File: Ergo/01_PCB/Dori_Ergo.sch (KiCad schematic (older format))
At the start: 208 parts, among them J1 TYPE-C-31-M12_13, J2 AVR-ISP-6_mod, J3 4PIN, J4 4PIN, J5 TYPE-C-31-M12_13, J6 AVR-ISP-6_mod, K1 KEYSW, K10 KEYSW, K11 KEYSW, K12 KEYSW, K13 KEYSW, K14 KEYSW, K15 KEYSW, K16 KEYSW, K17 KEYSW, K18 KEYSW, K19 KEYSW, K2 KEYSW, K20 KEYSW, K21 KEYSW, K22 KEYSW, K23 KEYSW, K24 KEYSW, K25 KEYSW, K26 KEYSW, K27 KEYSW, K28 KEYSW, K29 KEYSW, K3 KEYSW, K30 KEYSW, K31 KEYSW, K32 KEYSW, K33 KEYSW, K34 KEYSW, K35 KEYSW, K36 KEYSW, K37 KEYSW, K38 KEYSW, K39 KEYSW, K4 KEYSW, K40 KEYSW, K41 KEYSW, K42 KEYSW, K43 KEYSW, K44 KEYSW, K45 KEYSW, K46 KEYSW, K47 KEYSW, K48 KEYSW, K49 KEYSW, K5 KEYSW, K50 KEYSW, K51 KEYSW, K52 KEYSW, K53 KEYSW, K54 KEYSW, K55 KEYSW, K56 KEYSW, K6 KEYSW, K7 KEYSW, K8 KEYSW, K9 KEYSW, SW1 SW_PUSH, SW10 Rotary_Encoder_Switch, SW2 SW_PUSH, SW3 Rotary_Encoder_Switch, SW4 Rotary_Encoder_Switch, SW5 Rotary_Encoder_Switch, SW6 Rotary_Encoder_Switch, SW7 Rotary_Encoder_Switch, SW8 Rotary_Encoder_Switch, SW9 Rotary_Encoder_Switch, U1 ATMEGA32U4, U10 HOLE, U11 HOLE, U12 ATMEGA32U4, U13 HOLE, U14 HOLE, U15 HOLE, U16 HOLE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

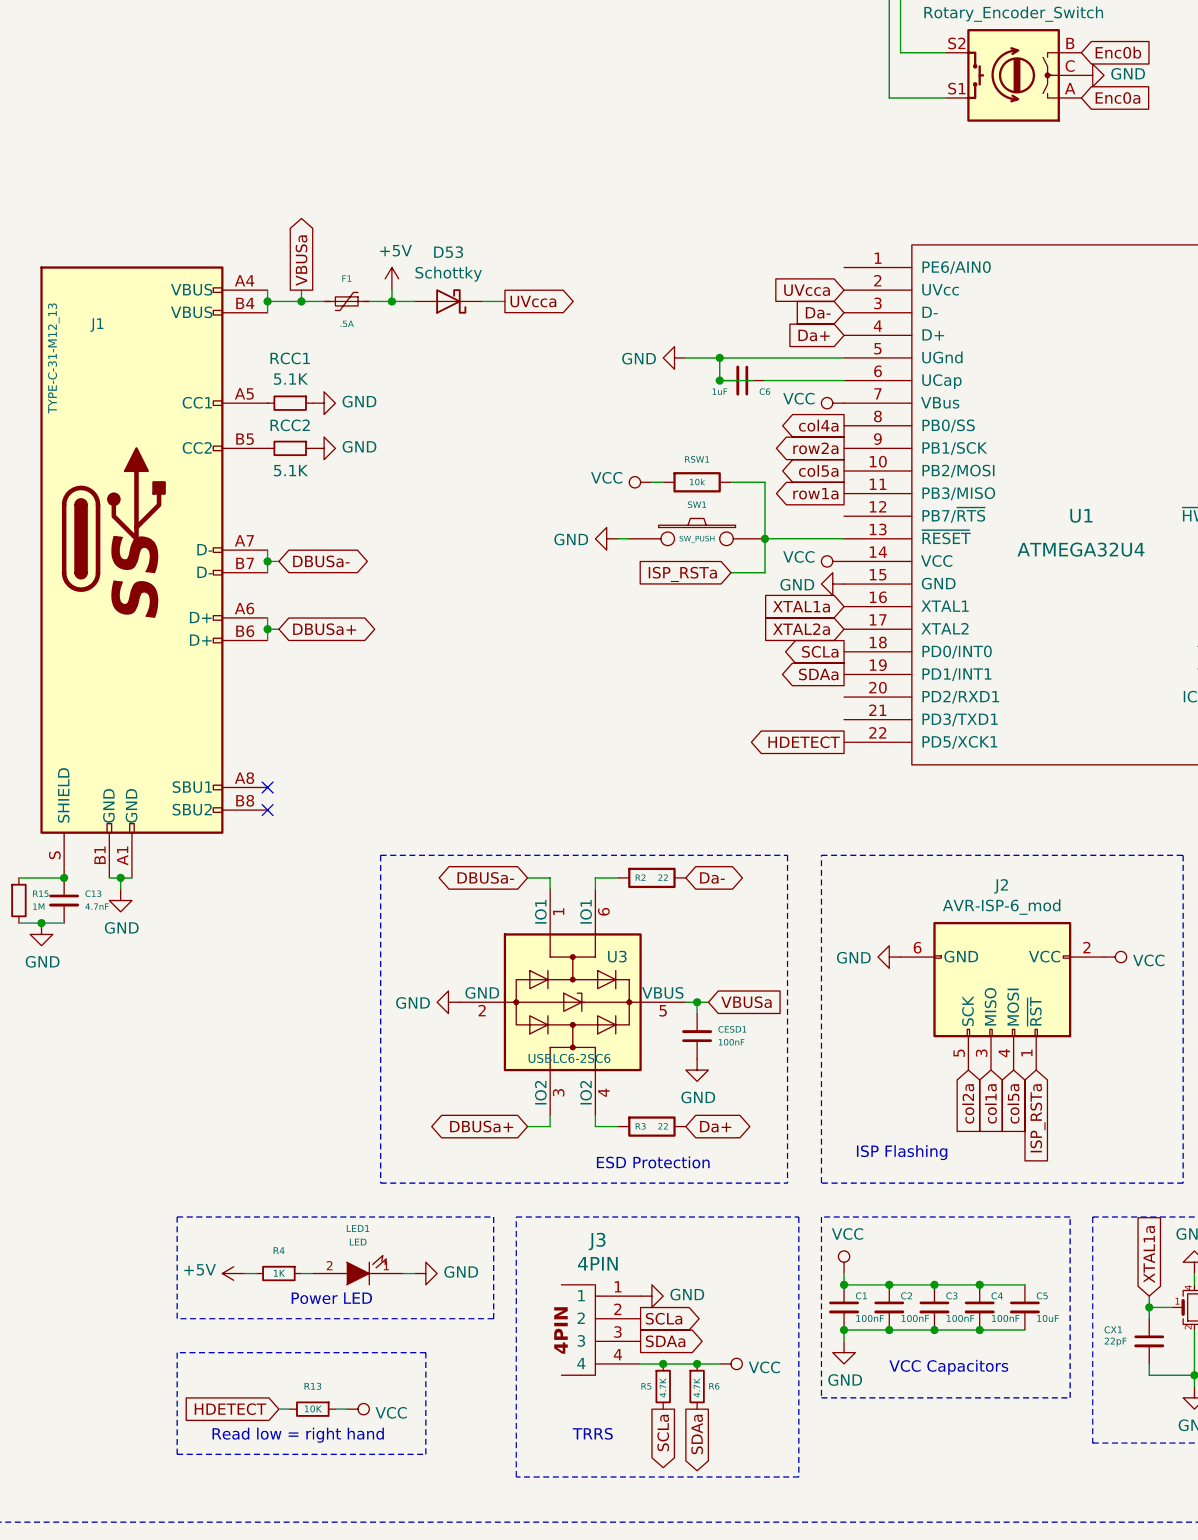
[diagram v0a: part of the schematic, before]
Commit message: Add ergo layout
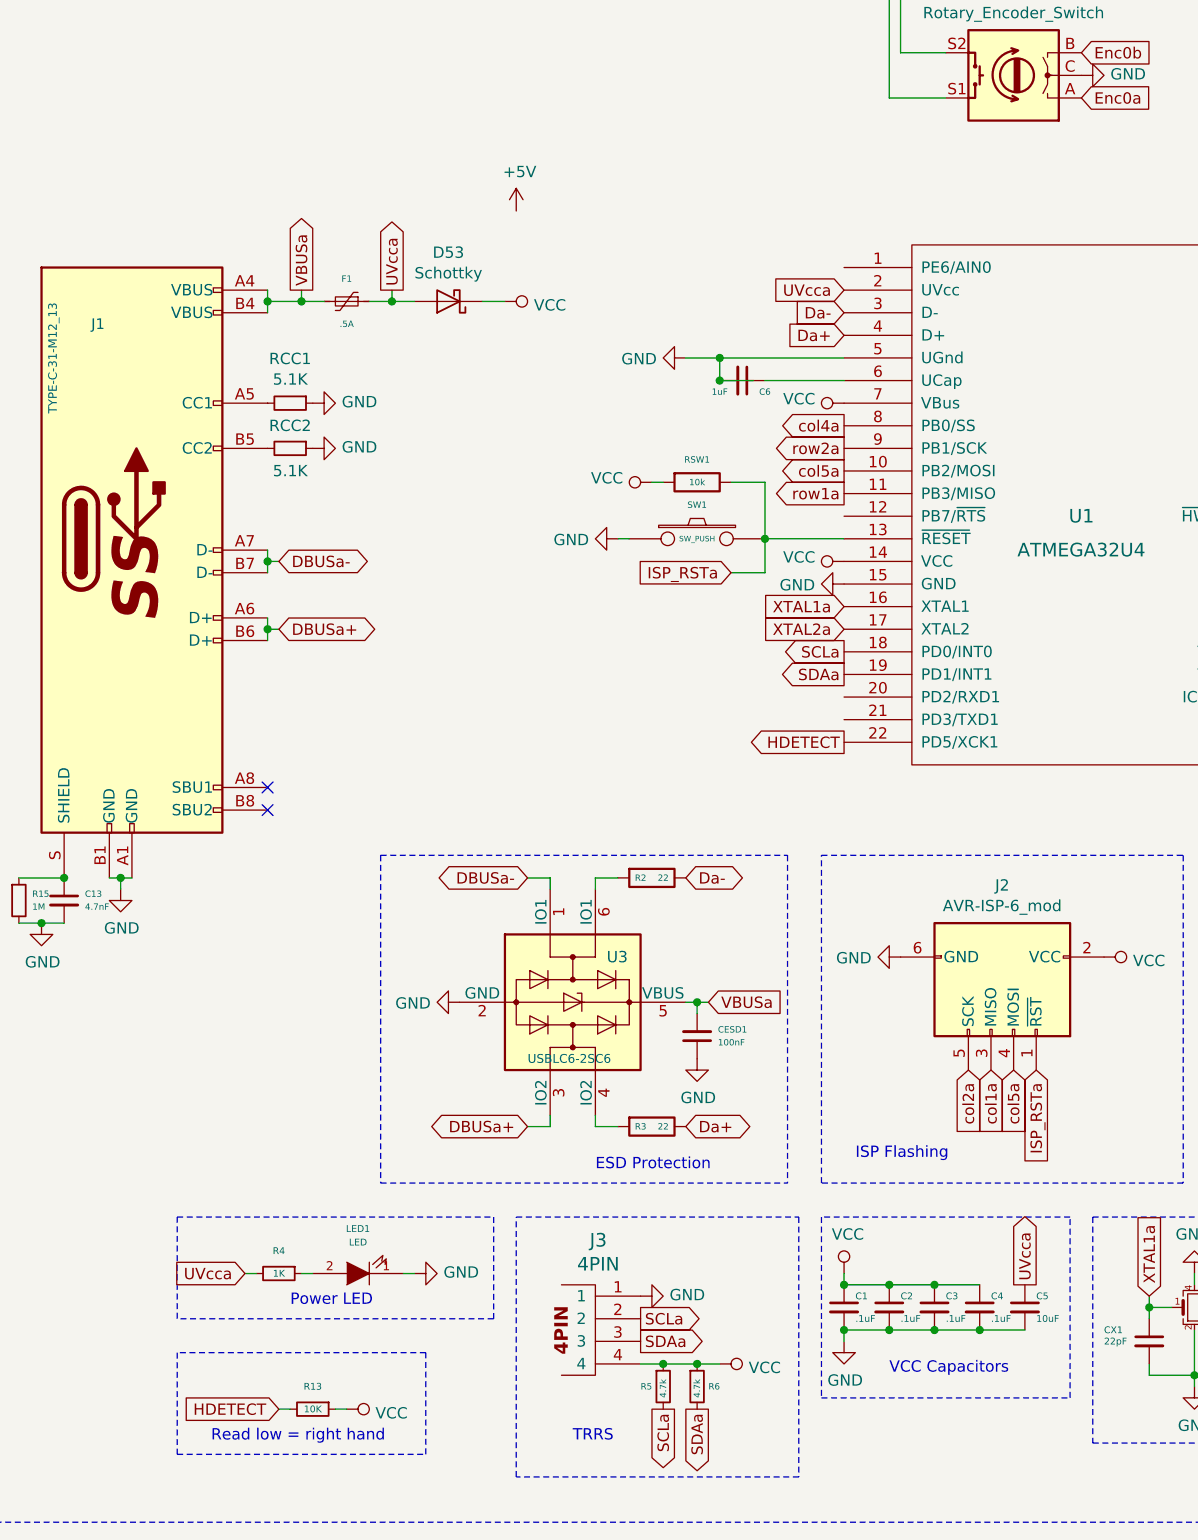
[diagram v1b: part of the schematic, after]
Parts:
- C1, C2, C3, C4: value 100nF -> .1uF
- R5, R6: value 4.7K -> 4.7k
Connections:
- net +5V: no longer D53.2 (A), F1.1, R4.2
- net UVcca: now also C5.1, D53.2 (A), F1.1, R4.2; no longer D53.1 (K)
- net VCC: now also D53.1 (K); no longer C5.1
